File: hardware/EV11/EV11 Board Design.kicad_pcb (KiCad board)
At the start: 4 copper layers, 66 x 99.3 mm, 127 parts, among them CN2 Conn_05x02_Female, CN3 Conn_01x06_Female, CN4 Conn_01x06_Female, CN5 Conn_02x05_Male, CN6 Conn_02x05_Male, CN7 Conn_02x05_Male, J1 Conn_01x02_Socket, J10 Conn_01x08_Socket, J2 AudioJack1, J3 Conn_01x06_Socket, J9 USB_C_Receptacle, SW1 TS-1037-A11B3-D2, SW3 TS-1037-A11B3-D2, SW4 SW_Push, SW5 SW_Push, SW6 SW_SPDT, U1 STM32F405RGTx, U11 ESP32-S3-WROOM-1-N8R2, U13 BM14B(0.8)-24DS-0.4V(53), U2 BQ21040DBV, U3 CH340C, U4 USBLC6-2P6, U5 M24C02-RMN6TP, U6 WM8960CGEFL/RV, U7 TPS63060, U8 STM32F072CBTx, Y1 Crystal_GND24

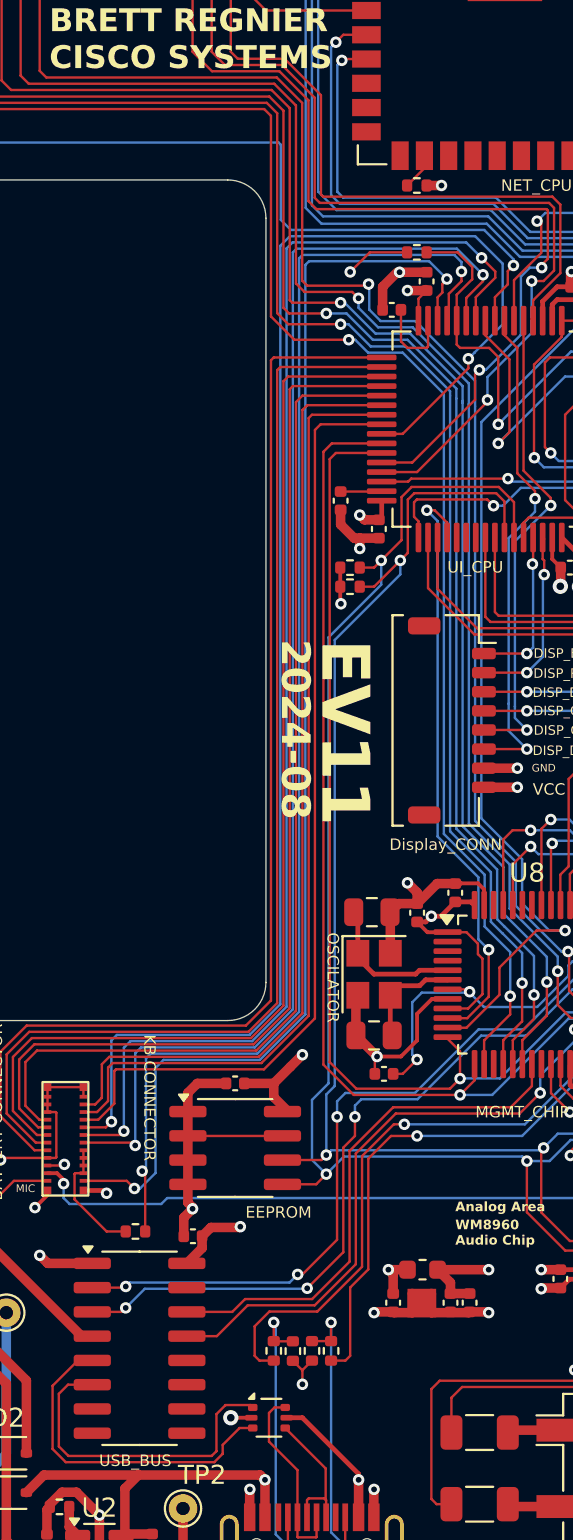
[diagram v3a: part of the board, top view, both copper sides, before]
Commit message: Added missing ground trace
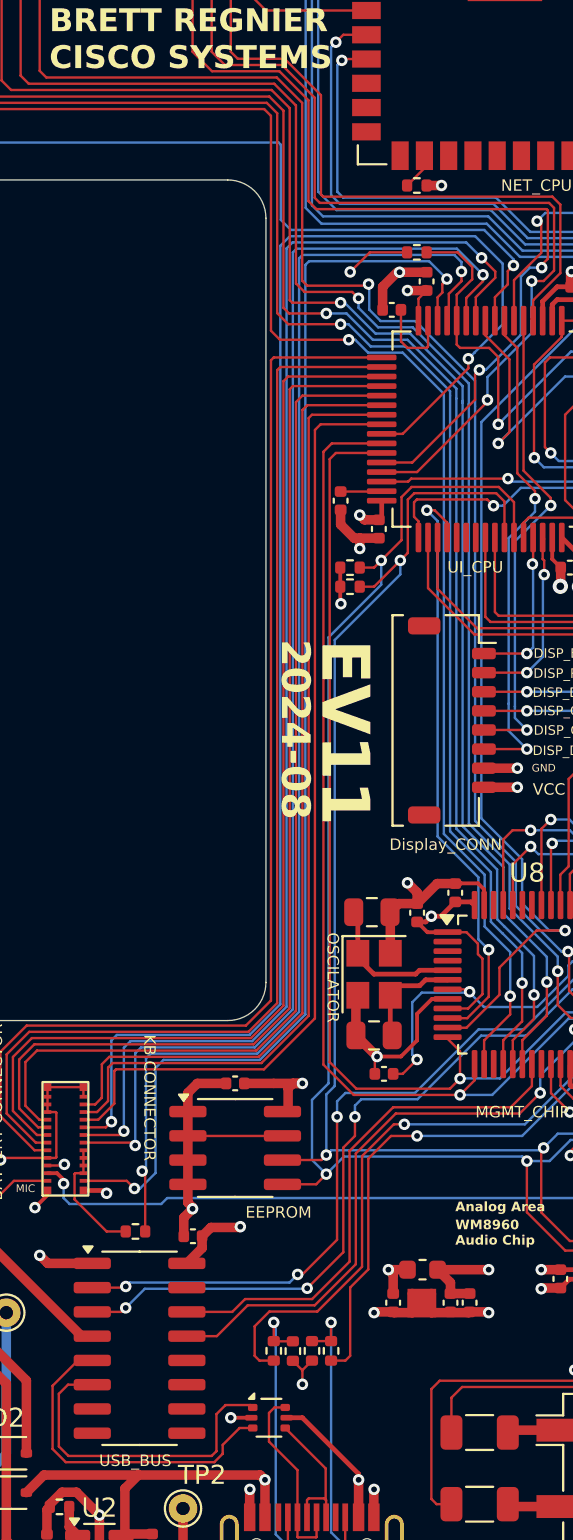
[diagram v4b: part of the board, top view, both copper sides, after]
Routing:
- net GND: track 591.1 -> 613.0 mm
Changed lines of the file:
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@@
 	)
 	(segment
+		(start 146.01 116.29)
+		(end 146.51 116.29)
+		(width 0.5)
+		(layer "F.Cu")
+		(net 2)
+	)
+	(segment
 		(start 178.26 139.54)
 		(end 178.26 138.58)
@@
 	)
 	(segment
-		(start 145.885 115.415)
-		(end 145.01 116.29)
-		(width 0.5)
-		(layer "F.Cu")
-		(net 2)
-	)
-	(segment
 		(start 152.585 76.365)
 		(end 152.585 75.215)
@@
 	)
 	(segment
+		(start 145.76 116.54)
+		(end 146.01 116.29)
+		(width 0.5)
+		(layer "F.Cu")
+		(net 2)
+	)
+	(segment
 		(start 141.26 124.91)
 		(end 140.46 125.71)
@@
 	)
 	(segment
-		(start 145.76 117.76)
-		(end 145.01 117.01)
-		(width 0.5)
-		(layer "F.Cu")
-		(net 2)
-	)
-	(segment
 		(start 160.547911 74.591721)
 		(end 159.843358 74.591721)
@@
 	)
 	(segment
-		(start 145.01 117.01)
-		(end 145.01 116.29)
-		(width 0.5)
-		(layer "F.Cu")
-		(net 2)
-	)
-	(segment
 		(start 129.96 124.04)
 		(end 129.96 122.84)
@@
 	)
 	(segment
-		(start 145.885 115.415)
-		(end 146.51 114.79)
+		(start 146.51 116.29)
+		(end 145.01 116.29)
 		(width 0.5)
 		(layer "F.Cu")
@@
 	)
 	(segment
+		(start 145.76 117.76)
+		(end 145.76 116.54)
+		(width 0.5)
+		(layer "F.Cu")
+		(net 2)
+	)
+	(segment
 		(start 149.86 51.24)
 		(end 148.81 51.24)
@@
 	)
 	(via
-		(at 146.51 114.79)
+		(at 146.51 116.29)
 		(size 0.6)
 		(drill 0.3)
@@
 	)
 	(segment
-		(start 146.45 114.85)
+		(start 146.32 114.85)
 		(end 130.2 114.85)
 		(width 0.5)
@@
 	)
 	(segment
-		(start 146.51 122.54)
-		(end 146.51 114.79)
-		(width 0.5)
-		(layer "In2.Cu")
-		(net 2)
-	)
-	(segment
 		(start 166.135 120.415)
 		(end 166.01 120.29)
@@
 	)
 	(segment
-		(start 146.51 114.79)
-		(end 146.45 114.85)
-		(width 0.5)
-		(layer "In2.Cu")
-		(net 2)
-	)
-	(segment
 		(start 156.86 104.64)
 		(end 153.01 100.79)
@@
 	)
 	(segment
+		(start 146.51 101.198514)
+		(end 146.51 116.29)
+		(width 0.5)
+		(layer "In2.Cu")
+		(net 2)
+	)
+	(segment
+		(start 146.51 115.04)
+		(end 146.32 114.85)
+		(width 0.5)
+		(layer "In2.Cu")
+		(net 2)
+	)
+	(segment
 		(start 178.26 114.04)
 		(end 178.01 114.29)
@@
 	)
 	(segment
-		(start 145.26 123.79)
-		(end 146.51 122.54)
-		(width 0.5)
-		(layer "In2.Cu")
-		(net 2)
-	)
-	(segment
 		(start 151.492343 74.787504)
 		(end 152.007911 74.787504)
@@
 	)
 	(segment
+		(start 146.51 116.29)
+		(end 146.51 122.54)
+		(width 0.5)
+		(layer "In2.Cu")
+		(net 2)
+	)
+	(segment
 		(start 163.26 105.54)
 		(end 163.76 106.04)
@@
 	)
 	(segment
+		(start 146.51 122.54)
+		(end 145.26 123.79)
+		(width 0.5)
+		(layer "In2.Cu")
+		(net 2)
+	)
+	(segment
 		(start 127.76 56.79)
 		(end 127.76 54.54)
@@
 	)
 	(segment
+		(start 130.2 114.85)
+		(end 129.96 115.09)
+		(width 0.5)
+		(layer "In2.Cu")
+		(net 2)
+	)
+	(segment
 		(start 178.01 139.29)
 		(end 178.01 114.79)
@@
 	)
 	(segment
-		(start 146.51 101.198514)
-		(end 146.51 114.79)
-		(width 0.5)
-		(layer "In2.Cu")
-		(net 2)
-	)
-	(segment
 		(start 143.26 123.79)
 		(end 145.26 123.79)
@@
 	)
 	(segment
+		(start 129.96 115.09)
+		(end 129.96 124.04)
+		(width 0.5)
+		(layer "In2.Cu")
+		(net 2)
+	)
+	(segment
 		(start 146.51 57.79)
 		(end 146.51 69.79)
@@
 	)
 	(segment
-		(start 130.2 114.85)
-		(end 129.96 115.09)
-		(width 0.5)
-		(layer "In2.Cu")
-		(net 2)
-	)
-	(segment
 		(start 178.01 104.79)
 		(end 178.01 114.79)
@@
 	)
 	(segment
-		(start 129.96 115.09)
-		(end 129.96 124.04)
-		(width 0.5)
-		(layer "In2.Cu")
-		(net 2)
-	)
-	(segment
 		(start 160.66 91.14)
 		(end 161.91 91.14)
@@
 	)
 	(via
-		(at 148.01 50.79)
+		(at 142.76 133.79)
 		(size 0.6)
 		(drill 0.3)
@@
 	)
 	(via
-		(at 152.01 105.79)
+		(at 148.01 50.79)
 		(size 0.6)
 		(drill 0.3)
@@
 	)
 	(via
-		(at 176.51 91.79)
+		(at 152.01 105.79)
 		(size 0.6)
 		(drill 0.3)
@@
 	)
 	(via
-		(at 142.76 133.79)
-		(size 0.8)
-		(drill 0.4)
+		(at 176.51 91.79)
+		(size 0.6)
+		(drill 0.3)
 		(layers "F.Cu" "B.Cu")
-		(free yes)
 		(net 4)
 	)
@@
 	)
 	(segment
+		(start 130.71 120.29)
+		(end 130.71 116.09)
+		(width 0.5)
+		(layer "In1.Cu")
+		(net 4)
+	)
+	(segment
 		(start 179.01 70.79)
 		(end 179.01 76.04)
@@
 	)
 	(segment
+		(start 147.35375 114.88375)
+		(end 150.41625 114.88375)
+		(width 0.5)
+		(layer "In1.Cu")
+		(net 4)
+	)
+	(segment
 		(start 148.510003 99.789997)
 		(end 148.51 99.79)
@@
 	)
 	(segment
-		(start 147.01 113.79)
-		(end 148.10375 114.88375)
-		(width 0.5)
-		(layer "In1.Cu")
-		(net 4)
-	)
-	(segment
 		(start 128.870197 130.929803)
 		(end 129.01 130.79)
@@
 	)
 	(segment
+		(start 131.26 115.54)
+		(end 146.635 115.54)
+		(width 0.5)
+		(layer "In1.Cu")
+		(net 4)
+	)
+	(segment
 		(start 147.01 51.79)
 		(end 147.01 52.79)
@@
 	)
 	(segment
+		(start 147.01 115.165)
+		(end 147.01 113.79)
+		(width 0.5)
+		(layer "In1.Cu")
+		(net 4)
+	)
+	(segment
 		(start 146.51 52.79)
 		(end 139.26 52.79)
@@
 	)
 	(segment
+		(start 147.01 114.54)
+		(end 147.35375 114.88375)
+		(width 0.5)
+		(layer "In1.Cu")
+		(net 4)
+	)
+	(segment
 		(start 132.76 130.54)
 		(end 132.76 125.29)
@@
 	)
 	(segment
+		(start 130.71 116.09)
+		(end 131.26 115.54)
+		(width 0.5)
+		(layer "In1.Cu")
+		(net 4)
+	)
+	(segment
 		(start 136.26 122.79)
 		(end 132.51 122.79)
@@
 	)
 	(segment
+		(start 146.635 115.54)
+		(end 147.01 115.165)
+		(width 0.5)
+		(layer "In1.Cu")
+		(net 4)
+	)
+	(segment
 		(start 144.01 136.29)
 		(end 143.76 136.54)
@@
 	)
 	(segment
-		(start 148.10375 114.88375)
-		(end 150.41625 114.88375)
-		(width 0.5)
-		(layer "In1.Cu")
-		(net 4)
-	)
-	(segment
 		(start 142.76 133.79)
 		(end 142.01 134.54)
@@
 	)
 	(segment
-		(start 128.76 65.29)
-		(end 128.013933 64.543933)
+		(start 144.8635 76.8935)
+		(end 144.8635 65.6435)
 		(width 0.127)
 		(layer "F.Cu")
@@
 	)
 	(segment
-		(start 146.083351 77.363351)
-		(end 144.8635 76.1435)
+		(start 148.936649 77.363351)
+		(end 145.333351 77.363351)
 		(width 0.127)
 		(layer "F.Cu")
@@
 	)
 	(segment
-		(start 144.8635 65.6435)
-		(end 144.51 65.29)
+		(start 157.387 112.674133)
+		(end 156.021133 114.04)
 		(width 0.127)
 		(layer "F.Cu")
@@
 	)
 	(segment
-		(start 148.936649 77.363351)
-		(end 146.083351 77.363351)
+		(start 157.387 111.7265)
+		(end 157.387 112.674133)
 		(width 0.127)
 		(layer "F.Cu")
@@
 	)
 	(segment
-		(start 157.387 112.674133)
-		(end 156.021133 114.04)
+		(start 156.021133 114.04)
+		(end 156.021133 115.367932)
 		(width 0.127)
 		(layer "F.Cu")
@@
 	)
 	(segment
-		(start 157.387 111.7265)
-		(end 157.387 112.674133)
+		(start 144.8635 65.6435)
+		(end 144.51 65.29)
 		(width 0.127)
 		(layer "F.Cu")
@@
 	)
 	(segment
-		(start 156.021133 114.04)
-		(end 156.021133 115.367932)
+		(start 145.333351 77.363351)
+		(end 144.8635 76.8935)
 		(width 0.127)
 		(layer "F.Cu")
@@
 	)
 	(segment
-		(start 128.013933 64.543933)
-		(end 128.013933 62.789493)
+		(start 128.76 65.29)
+		(end 128.013933 64.543933)
 		(width 0.127)
 		(layer "F.Cu")
@@
 	)
 	(segment
-		(start 144.51 65.29)
-		(end 128.76 65.29)
+		(start 128.013933 64.543933)
+		(end 128.013933 62.789493)
 		(width 0.127)
 		(layer "F.Cu")
@@
 	)
 	(segment
-		(start 144.8635 76.1435)
-		(end 144.8635 65.6435)
+		(start 144.51 65.29)
+		(end 128.76 65.29)
 		(width 0.127)
 		(layer "F.Cu")
@@
 		(min_thickness 0.25)
 		(filled_areas_thickness no)
-		(fill yes
+		(fill
 			(thermal_gap 0.5)
 			(thermal_bridge_width 0.5)

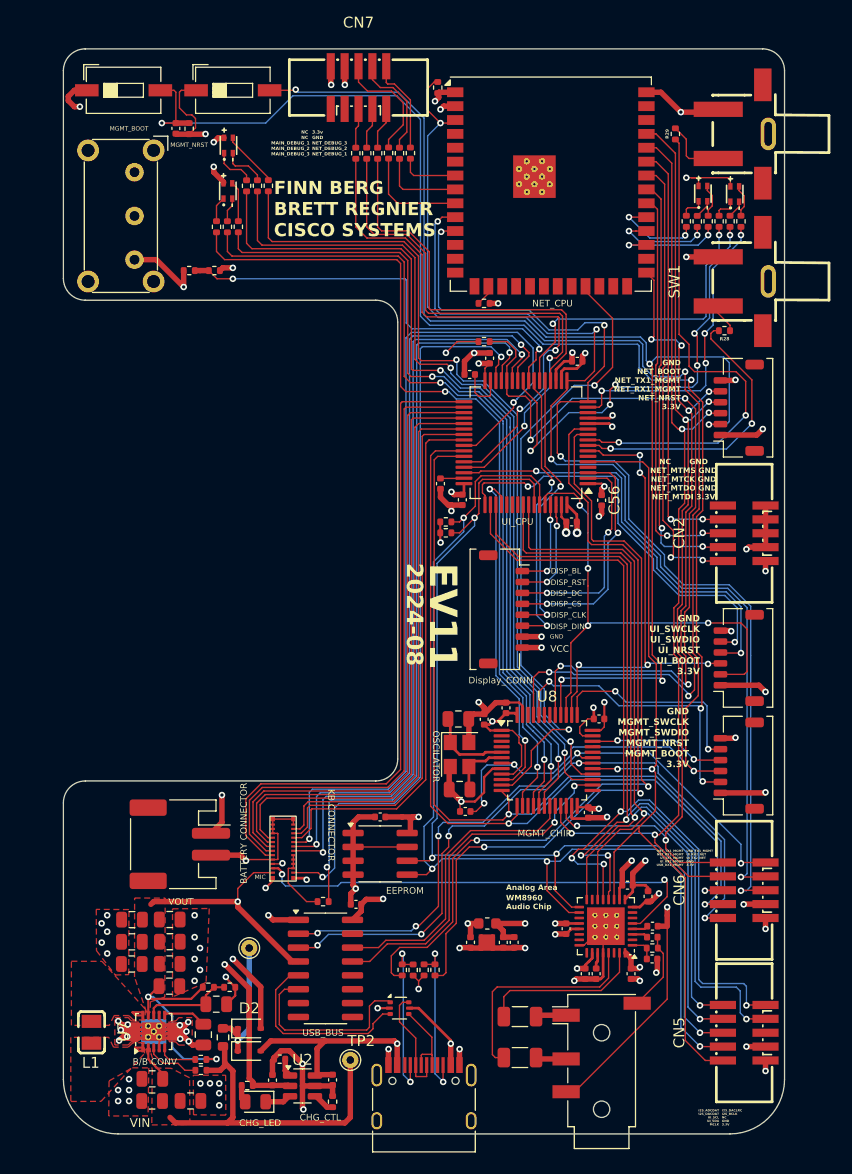
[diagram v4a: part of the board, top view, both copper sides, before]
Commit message: Clean up traces, add missing 3d models
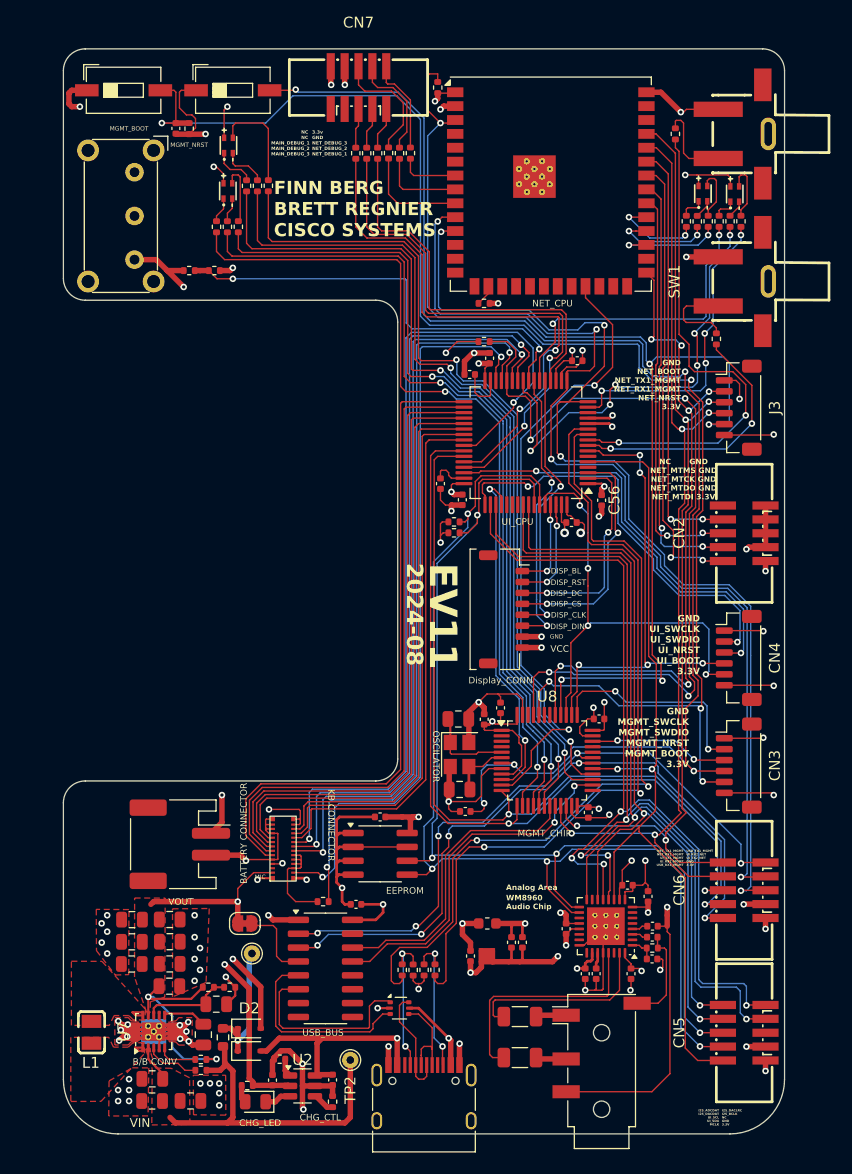
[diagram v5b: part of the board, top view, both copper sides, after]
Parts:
- added JP3: SolderJumper_2_Bridged, Jumper:SolderJumper-2_P1.3mm_Bridged_RoundedPad1.0x1.5mm, F.Cu at (130.6, 126.0)
- CN3, CN4, J3: footprint Connector_JST:JST_SHL_SM06B-SHLS-TF_1x06-1MP_P1.00mm_Horizontal -> Connector_JST:JST_SH_BM06B-SRSS-TB_1x06-1MP_P1.00mm_Vertical
- moved C10 1.25 mm to (151.3, 129.0)
- moved NT1 1.25 mm to (152.8, 129.0)
- moved R28 1.05 mm to (173.8, 72.5), turned to 90 degrees
- moved C8 0.75 mm to (156.0, 127.8)
- moved C9 0.75 mm to (155.0, 127.8)
- moved R7 0.75 mm to (149.8, 89.3)
- moved R8 0.75 mm to (149.8, 90.3)
- moved TP1 0.56 mm to (131.3, 128.8)
- moved C26 0.50 mm to (154.0, 106.3)
- moved C12 0.06 mm to (160.5, 89.3)
- moved C11 0.05 mm to (161.0, 74.5)
- turned CN3 to -90 degrees
- turned CN4 to -90 degrees
- turned J3 to -90 degrees
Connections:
- CN3 pad 2: /MGMT_BOOT -> /MGMT_SWCLK
- CN3 pad 3: /MGMT_NRST -> /MGMT_SWDIO
- CN3 pad 4: /MGMT_SWDIO -> /MGMT_NRST
- CN3 pad 5: /MGMT_SWCLK -> /MGMT_BOOT
- CN4 pad 2: /UI_BOOT -> /UI_SWCLK
- CN4 pad 3: /UI_NRST -> /UI_SWDIO
- CN4 pad 4: /UI_SWDIO -> /UI_NRST
- CN4 pad 5: /UI_SWCLK -> /UI_BOOT
- J3 pad 2: /NET_NRST -> /NET_BOOT
- J3 pad 3: /NET_RX1_MGMT -> /NET_TX1_MGMT
- J3 pad 4: /NET_TX1_MGMT -> /NET_RX1_MGMT
- J3 pad 5: /NET_BOOT -> /NET_NRST
- U3 pad 4: +3.3V -> Net-(JP3-A)
- U6 pad 5: /KB_MIC -> unconnected-(U6-RINPUT1-Pad5)
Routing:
- net /KB_MIC: track 43.1 -> 0.00 mm, vias 2 -> 0
- net GND: track 613.0 -> 630.5 mm, vias 69 -> 70
- net GNDA: track 69.5 -> 78.6 mm
- net Net-(JP3-A): track 0.00 -> 7.16 mm
- net +3.3V: track 487.6 -> 493.9 mm
- net /PTT_BTN: track 2.71 -> 8.08 mm
- net /MIC_N: track 20.3 -> 24.6 mm
- net Net-(D4---Pad3): track 5.22 -> 9.38 mm
- net /UI_BOOT: track 46.5 -> 42.5 mm
- net /KB_LED: track 6.39 -> 9.83 mm
- net Net-(U6-HP_L): track 15.1 -> 17.7 mm
- net Net-(D7---Pad3): track 3.00 -> 5.55 mm
- net Net-(J9-CC1): track 15.6 -> 13.4 mm
- net Net-(J9-CC2): track 15.6 -> 13.4 mm
- net Net-(U1-PC0): track 26.8 -> 24.8 mm
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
